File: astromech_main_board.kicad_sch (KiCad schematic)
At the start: 88 parts, among them IC1 MAX11645EUA+, J1 Screw_Terminal_01x02, J10 Conn_01x05, J11 Conn_01x06, J12 Conn_01x04, J13 Conn_01x05, J14 Conn_01x04, J15 Conn_01x04, J19 Conn_01x04, J2 Screw_Terminal_01x02, J20 Conn_01x04, J21 Conn_01x04, J3 Screw_Terminal_01x02, J4 IO_XPAND, J5 Conn_01x06, J6 Conn_01x06, J7 Conn_01x08, J8 Conn_01x03, J9 Conn_01x06, U1 TCA9554DW, U10 LS7366R, U11 LS7366R, U2 TCA9554DW, U3 NCP1117-3.3_SOT223, U4 NCP1117-5.0_TO252, U5 SC16IS752IPW_128, U6 TXB0108PW, U7 TCA9517ADGK, U8 74HC14, U9 LS7366R, Y1 Crystal, Y2 Crystal

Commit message: made encoders 3v3
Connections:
- net 3V3: now also C10.2, C11.2, C12.2, U10.14 (VDD), U11.14 (VDD), U9.14 (VDD)
- net 5V: no longer C10.2, C11.2, C12.2, U10.14 (VDD), U11.14 (VDD), U9.14 (VDD)
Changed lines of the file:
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@@
 	)
 	(symbol
+		(lib_id "power:+3.3V")
+		(at 265.43 50.8 0)
+		(unit 1)
+		(exclude_from_sim no)
+		(in_bom yes)
+		(on_board yes)
+		(dnp no)
+		(property "Reference" "#PWR087"
+			(at 265.43 54.61 0)
+			(effects
+				(font
+					(size 1.27 1.27)
+				)
+				(hide yes)
+			)
+		)
+		(property "Value" "3V3"
+			(at 265.43 46.99 0)
+			(effects
+				(font
+					(size 1.27 1.27)
+				)
+			)
+		)
+		(property "Footprint" ""
+			(at 265.43 50.8 0)
+			(effects
+				(font
+					(size 1.27 1.27)
+				)
+				(hide yes)
+			)
+		)
+		(property "Datasheet" ""
+			(at 265.43 50.8 0)
+			(effects
+				(font
+					(size 1.27 1.27)
+				)
+				(hide yes)
+			)
+		)
+		(property "Description" "Power symbol creates a global label with name \"+3.3V\""
+			(at 265.43 50.8 0)
+			(effects
+				(font
+					(size 1.27 1.27)
+				)
+				(hide yes)
+			)
+		)
+		(pin "1"
+		)
+		(instances
+			(project "astromech_main_board"
+				(path "/3ed70c37-1dc6-4761-9813-fca49ce12494"
+					(reference "#PWR087")
+					(unit 1)
+				)
+			)
+		)
+	)
+	(symbol
 		(lib_id "Device:C_Small")
 		(at -68.58 176.53 90)
@@
 	)
 	(symbol
+		(lib_id "power:+3.3V")
+		(at 280.67 91.44 0)
+		(unit 1)
+		(exclude_from_sim no)
+		(in_bom yes)
+		(on_board yes)
+		(dnp no)
+		(property "Reference" "#PWR050"
+			(at 280.67 95.25 0)
+			(effects
+				(font
+					(size 1.27 1.27)
+				)
+				(hide yes)
+			)
+		)
+		(property "Value" "3V3"
+			(at 280.67 87.63 0)
+			(effects
+				(font
+					(size 1.27 1.27)
+				)
+			)
+		)
+		(property "Footprint" ""
+			(at 280.67 91.44 0)
+			(effects
+				(font
+					(size 1.27 1.27)
+				)
+				(hide yes)
+			)
+		)
+		(property "Datasheet" ""
+			(at 280.67 91.44 0)
+			(effects
+				(font
+					(size 1.27 1.27)
+				)
+				(hide yes)
+			)
+		)
+		(property "Description" "Power symbol creates a global label with name \"+3.3V\""
+			(at 280.67 91.44 0)
+			(effects
+				(font
+					(size 1.27 1.27)
+				)
+				(hide yes)
+			)
+		)
+		(pin "1"
+		)
+		(instances
+			(project "astromech_main_board"
+				(path "/3ed70c37-1dc6-4761-9813-fca49ce12494"
+					(reference "#PWR050")
+					(unit 1)
+				)
+			)
+		)
+	)
+	(symbol
 		(lib_id "LS7366R:LS7366R")
 		(at 246.38 114.3 0)
@@
 	)
 	(symbol
-		(lib_id "power:+3.3V")
-		(at 279.4 134.62 0)
-		(unit 1)
-		(exclude_from_sim no)
-		(in_bom yes)
-		(on_board yes)
-		(dnp no)
-		(property "Reference" "#PWR054"
-			(at 279.4 138.43 0)
-			(effects
-				(font
-					(size 1.27 1.27)
-				)
-				(hide yes)
-			)
-		)
-		(property "Value" "5V"
-			(at 279.4 130.81 0)
-			(effects
-				(font
-					(size 1.27 1.27)
-				)
-			)
-		)
-		(property "Footprint" ""
-			(at 279.4 134.62 0)
-			(effects
-				(font
-					(size 1.27 1.27)
-				)
-				(hide yes)
-			)
-		)
-		(property "Datasheet" ""
-			(at 279.4 134.62 0)
-			(effects
-				(font
-					(size 1.27 1.27)
-				)
-				(hide yes)
-			)
-		)
-		(property "Description" "Power symbol creates a global label with name \"+3.3V\""
-			(at 279.4 134.62 0)
-			(effects
-				(font
-					(size 1.27 1.27)
-				)
-				(hide yes)
-			)
-		)
-		(pin "1"
-		)
-		(instances
-			(project "astromech_main_board"
-				(path "/3ed70c37-1dc6-4761-9813-fca49ce12494"
-					(reference "#PWR054")
-					(unit 1)
-				)
-			)
-		)
-	)
-	(symbol
 		(lib_id "power:GND")
 		(at 185.42 242.57 0)
@@
 	)
 	(symbol
-		(lib_id "power:+3.3V")
-		(at 265.43 50.8 0)
-		(unit 1)
-		(exclude_from_sim no)
-		(in_bom yes)
-		(on_board yes)
-		(dnp no)
-		(property "Reference" "#PWR050"
-			(at 265.43 54.61 0)
-			(effects
-				(font
-					(size 1.27 1.27)
-				)
-				(hide yes)
-			)
-		)
-		(property "Value" "5V"
-			(at 265.43 46.99 0)
-			(effects
-				(font
-					(size 1.27 1.27)
-				)
-			)
-		)
-		(property "Footprint" ""
-			(at 265.43 50.8 0)
-			(effects
-				(font
-					(size 1.27 1.27)
-				)
-				(hide yes)
-			)
-		)
-		(property "Datasheet" ""
-			(at 265.43 50.8 0)
-			(effects
-				(font
-					(size 1.27 1.27)
-				)
-				(hide yes)
-			)
-		)
-		(property "Description" "Power symbol creates a global label with name \"+3.3V\""
-			(at 265.43 50.8 0)
-			(effects
-				(font
-					(size 1.27 1.27)
-				)
-				(hide yes)
-			)
-		)
-		(pin "1"
-		)
-		(instances
-			(project "astromech_main_board"
-				(path "/3ed70c37-1dc6-4761-9813-fca49ce12494"
-					(reference "#PWR050")
-					(unit 1)
-				)
-			)
-		)
-	)
-	(symbol
 		(lib_id "74xx:74HC14")
 		(at 177.8 107.95 0)
@@
 	(symbol
 		(lib_id "power:+3.3V")
-		(at 280.67 91.44 0)
-		(unit 1)
-		(exclude_from_sim no)
-		(in_bom yes)
-		(on_board yes)
-		(dnp no)
-		(property "Reference" "#PWR052"
-			(at 280.67 95.25 0)
-			(effects
-				(font
-					(size 1.27 1.27)
-				)
-				(hide yes)
-			)
-		)
-		(property "Value" "5V"
-			(at 280.67 87.63 0)
-			(effects
-				(font
-					(size 1.27 1.27)
-				)
-			)
-		)
-		(property "Footprint" ""
-			(at 280.67 91.44 0)
-			(effects
-				(font
-					(size 1.27 1.27)
-				)
-				(hide yes)
-			)
-		)
-		(property "Datasheet" ""
-			(at 280.67 91.44 0)
-			(effects
-				(font
-					(size 1.27 1.27)
-				)
-				(hide yes)
-			)
-		)
-		(property "Description" "Power symbol creates a global label with name \"+3.3V\""
-			(at 280.67 91.44 0)
-			(effects
-				(font
-					(size 1.27 1.27)
-				)
-				(hide yes)
-			)
-		)
-		(pin "1"
-		)
-		(instances
-			(project "astromech_main_board"
-				(path "/3ed70c37-1dc6-4761-9813-fca49ce12494"
-					(reference "#PWR052")
-					(unit 1)
-				)
-			)
-		)
-	)
-	(symbol
-		(lib_id "power:+3.3V")
 		(at 270.51 220.98 0)
 		(unit 1)
@@
 					(unit 1)
 				)
+			)
+		)
+	)
+	(symbol
+		(lib_id "power:+3.3V")
+		(at 279.4 134.62 0)
+		(unit 1)
+		(exclude_from_sim no)
+		(in_bom yes)
+		(on_board yes)
+		(dnp no)
+		(property "Reference" "#PWR052"
+			(at 279.4 138.43 0)
+			(effects
+				(font
+					(size 1.27 1.27)
+				)
+				(hide yes)
+			)
+		)
+		(property "Value" "3V3"
+			(at 279.4 130.81 0)
+			(effects
+				(font
+					(size 1.27 1.27)
+				)
+			)
+		)
+		(property "Footprint" ""
+			(at 279.4 134.62 0)
+			(effects
+				(font
+					(size 1.27 1.27)
+				)
+				(hide yes)
+			)
+		)
+		(property "Datasheet" ""
+			(at 279.4 134.62 0)
+			(effects
+				(font
+					(size 1.27 1.27)
+				)
+				(hide yes)
+			)
+		)
+		(property "Description" "Power symbol creates a global label with name \"+3.3V\""
+			(at 279.4 134.62 0)
+			(effects
+				(font
+					(size 1.27 1.27)
+				)
+				(hide yes)
+			)
+		)
+		(pin "1"
+		)
+		(instances
+			(project "astromech_main_board"
+				(path "/3ed70c37-1dc6-4761-9813-fca49ce12494"
+					(reference "#PWR052")
+					(unit 1)
+				)

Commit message: layout mostly done
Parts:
- removed R7: R_Small_US, Resistor_SMD:R_1206_3216Metric, symbol Device:R_Small_US
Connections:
- net 3V3: now also R22.2; no longer R22.1
- net IO14: now also R22.1; no longer R22.2
- net IO18: now also U8.12; no longer U8.4
- net at J4.14 (Pin_14), U2.10 (P5): no longer R15.1
- net at J4.15 (Pin_15), U2.11 (P6): no longer R18.1
- net at J4.16 (Pin_16), U2.12 (P7): no longer R19.1
- net at J4.13 (Pin_13), U2.9 (P4): no longer R14.1
- net at J4.1 (Pin_1), U1.4 (P0): now also R19.1
- net at J4.2 (Pin_2), U1.5 (P1): now also R18.1
- net at J4.3 (Pin_3), U1.6 (P2): now also R15.1
- net at J4.4 (Pin_4), U1.7 (P3): now also R14.1
- net at U8.13: now also JP13.3 (B)
- net at U8.3: no longer JP13.3 (B)
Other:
- moved on the sheet: J4, R22

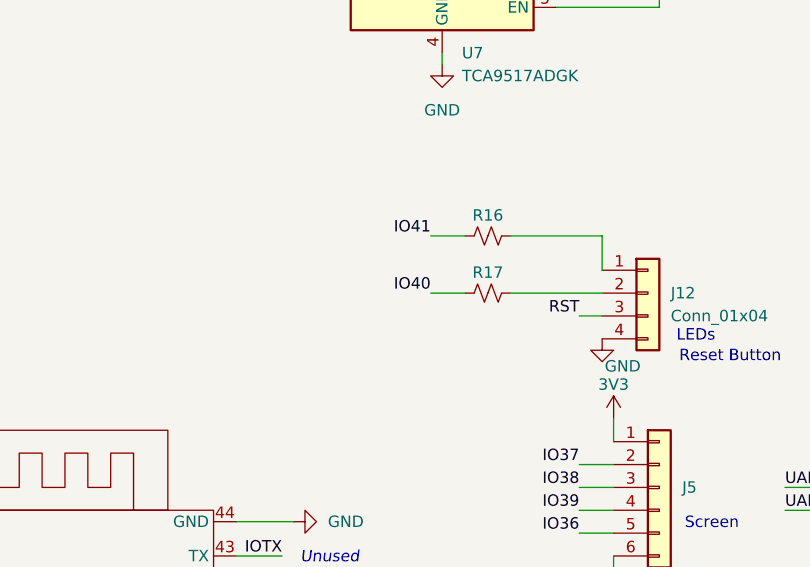
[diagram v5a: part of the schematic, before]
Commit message: main routing done
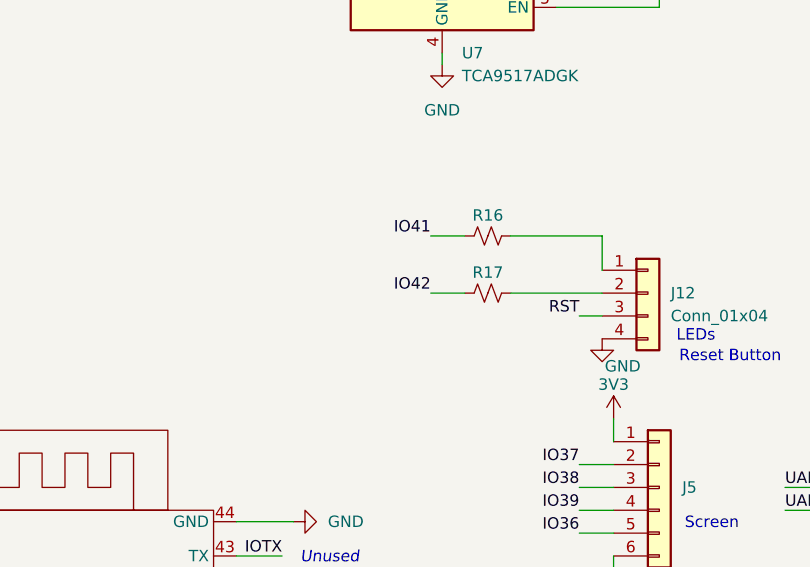
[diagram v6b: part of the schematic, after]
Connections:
- net IO40: no longer R17.1
- net IO42: now also R17.1
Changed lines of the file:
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@@
+		)
+	)
+	(label "IO42"
+		(at 165.1 187.96 180)
+		(fields_autoplaced yes)
+		(effects
+			(font
+				(size 1.27 1.27)
+			)
+			(justify right bottom)
 		)
 	)
@@
 		(fields_autoplaced yes)
 		(effects
-			(font
-				(size 1.27 1.27)
-			)
-			(justify right bottom)
-		)
-	)
-	(label "IO40"
-		(at 165.1 187.96 180)
-		(fields_autoplaced yes)
-		(effects

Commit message: 3v3 routed
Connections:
- net IO17: now also J7.5 (Pin_5); no longer J7.1 (Pin_1)
- net IO21: now also J7.1 (Pin_1); no longer J7.3 (Pin_3)
- net IO35: now also J7.3 (Pin_3); no longer J7.4 (Pin_4)
- net IO40: now also J7.6 (Pin_6); no longer J7.5 (Pin_5)
- net IO45: now also J7.2 (Pin_2); no longer J7.6 (Pin_6)
- net IO8: now also J7.4 (Pin_4); no longer J7.2 (Pin_2)
- net IORX: now also J7.7 (Pin_7); no longer J7.8 (Pin_8)
- net IOTX: now also J7.8 (Pin_8); no longer J7.7 (Pin_7)
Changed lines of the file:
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@@
 	(wire
 		(pts
+			(xy 160.02 302.26) (xy 162.56 302.26)
+		)
+		(stroke
+			(width 0)
+			(type default)
+		)
+	)
+	(wire
+		(pts
 			(xy 76.2 146.05) (xy 73.66 146.05)
 		)
@@
 		)
 	)
+	(wire
+		(pts
+			(xy 160.02 299.72) (xy 162.56 299.72)
+		)
+		(stroke
+			(width 0)
+			(type default)
+		)
+	)
 	(polyline
 		(pts
@@
 	(wire
 		(pts
-			(xy 46.99 35.56) (xy 53.34 35.56)
+			(xy 160.02 294.64) (xy 162.56 294.64)
 		)
 		(stroke
@@
 	(wire
 		(pts
-			(xy 143.51 224.79) (xy 148.59 224.79)
+			(xy 46.99 35.56) (xy 53.34 35.56)
 		)
 		(stroke
@@
 	(wire
 		(pts
-			(xy 205.74 90.17) (xy 205.74 91.44)
+			(xy 143.51 224.79) (xy 148.59 224.79)
 		)
 		(stroke
@@
 	(wire
 		(pts
-			(xy 39.37 133.35) (xy 53.34 133.35)
+			(xy 205.74 90.17) (xy 205.74 91.44)
 		)
 		(stroke
@@
 	(wire
 		(pts
-			(xy 158.75 312.42) (xy 162.56 312.42)
+			(xy 39.37 133.35) (xy 53.34 133.35)
 		)
 		(stroke
@@
 	(wire
 		(pts
-			(xy 158.75 297.18) (xy 162.56 297.18)
-		)
-		(stroke
-			(width 0)
-			(type default)
-		)
-	)
-	(wire
-		(pts
 			(xy 149.86 138.43) (xy 149.86 139.7)
 		)
@@
 	(wire
 		(pts
-			(xy 158.75 302.26) (xy 162.56 302.26)
-		)
-		(stroke
-			(width 0)
-			(type default)
-		)
-	)
-	(wire
-		(pts
 			(xy 22.86 248.92) (xy 41.91 248.92)
 		)
@@
 	(wire
 		(pts
+			(xy 160.02 304.8) (xy 162.56 304.8)
+		)
+		(stroke
+			(width 0)
+			(type default)
+		)
+	)
+	(wire
+		(pts
 			(xy 127 115.57) (xy 133.35 115.57)
 		)
@@
 	(wire
 		(pts
+			(xy 160.02 312.42) (xy 162.56 312.42)
+		)
+		(stroke
+			(width 0)
+			(type default)
+		)
+	)
+	(wire
+		(pts
 			(xy 181.61 214.63) (xy 185.42 214.63)
 		)
@@
 	(wire
 		(pts
-			(xy 158.75 304.8) (xy 162.56 304.8)
-		)
-		(stroke
-			(width 0)
-			(type default)
-		)
-	)
-	(wire
-		(pts
 			(xy 144.78 293.37) (xy 143.51 293.37)
 		)
@@
 	(wire
 		(pts
+			(xy 160.02 307.34) (xy 162.56 307.34)
+		)
+		(stroke
+			(width 0)
+			(type default)
+		)
+	)
+	(wire
+		(pts
 			(xy 278.13 135.89) (xy 279.4 135.89)
 		)
@@
 	(wire
 		(pts
-			(xy 158.75 309.88) (xy 162.56 309.88)
-		)
-		(stroke
-			(width 0)
-			(type default)
-		)
-	)
-	(wire
-		(pts
 			(xy 240.03 203.2) (xy 257.81 203.2)
 		)
@@
 	(wire
 		(pts
+			(xy 160.02 309.88) (xy 162.56 309.88)
+		)
+		(stroke
+			(width 0)
+			(type default)
+		)
+	)
+	(wire
+		(pts
 			(xy 214.63 121.92) (xy 228.6 121.92)
 		)
@@
 	(wire
 		(pts
+			(xy 160.02 297.18) (xy 162.56 297.18)
+		)
+		(stroke
+			(width 0)
+			(type default)
+		)
+	)
+	(wire
+		(pts
 			(xy -57.15 165.1) (xy -57.15 163.83)
 		)
@@
 	(wire
 		(pts
-			(xy 158.75 299.72) (xy 162.56 299.72)
-		)
-		(stroke
-			(width 0)
-			(type default)
-		)
-	)
-	(wire
-		(pts
 			(xy 240.03 185.42) (xy 257.81 185.42)
 		)
@@
 	(wire
 		(pts
-			(xy 158.75 294.64) (xy 162.56 294.64)
-		)
-		(stroke
-			(width 0)
-			(type default)
-		)
-	)
-	(wire
-		(pts
 			(xy 264.16 153.67) (xy 281.94 153.67)
 		)
@@
 	(wire
 		(pts
-			(xy 158.75 307.34) (xy 162.56 307.34)
-		)
-		(stroke
-			(width 0)
-			(type default)
-		)
-	)
-	(wire
-		(pts
 			(xy 73.66 182.88) (xy 86.36 182.88)
 		)
@@
 	)
 	(label "IO40"
-		(at 158.75 304.8 180)
+		(at 160.02 307.34 180)
 		(fields_autoplaced yes)
 		(effects
@@
 	)
 	(label "IO8"
-		(at 158.75 297.18 180)
+		(at 160.02 302.26 180)
 		(fields_autoplaced yes)
 		(effects
@@
 	)
 	(label "IORX"
-		(at 158.75 312.42 180)
+		(at 160.02 309.88 180)
 		(fields_autoplaced yes)
 		(effects
@@
 	)
 	(label "IO35"
-		(at 158.75 302.26 180)
+		(at 160.02 299.72 180)
 		(fields_autoplaced yes)
 		(effects
@@
 	)
 	(label "IO17"
-		(at 158.75 294.64 180)
+		(at 160.02 304.8 180)
 		(fields_autoplaced yes)
 		(effects
@@
 	)
 	(label "IOTX"
-		(at 158.75 309.88 180)
+		(at 160.02 312.42 180)
 		(fields_autoplaced yes)
 		(effects
@@
 	)
 	(label "IO21"
-		(at 158.75 299.72 180)
+		(at 160.02 294.64 180)
 		(fields_autoplaced yes)
 		(effects
@@
 	)
 	(label "IO45"
-		(at 158.75 307.34 180)
+		(at 160.02 297.18 180)
 		(fields_autoplaced yes)
 		(effects
